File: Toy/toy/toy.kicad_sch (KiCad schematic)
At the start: 13 parts, among them J1 Conn_01x07_Pin, J2 Conn_01x03_Pin

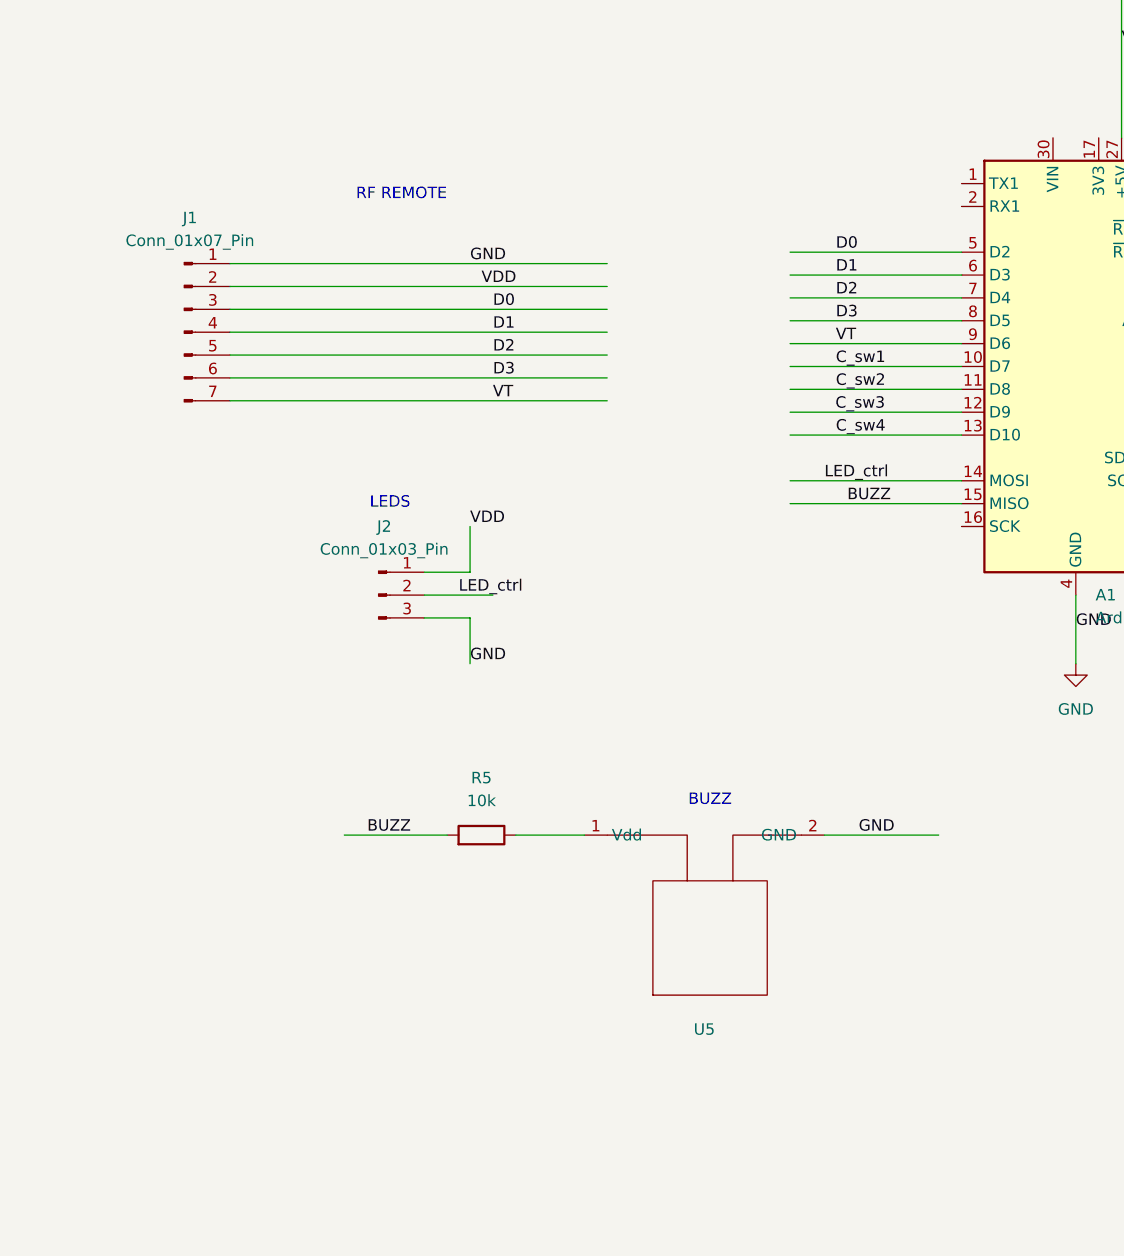
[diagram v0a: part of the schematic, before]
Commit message: V2
resistors changed
routing strategy
added more leds
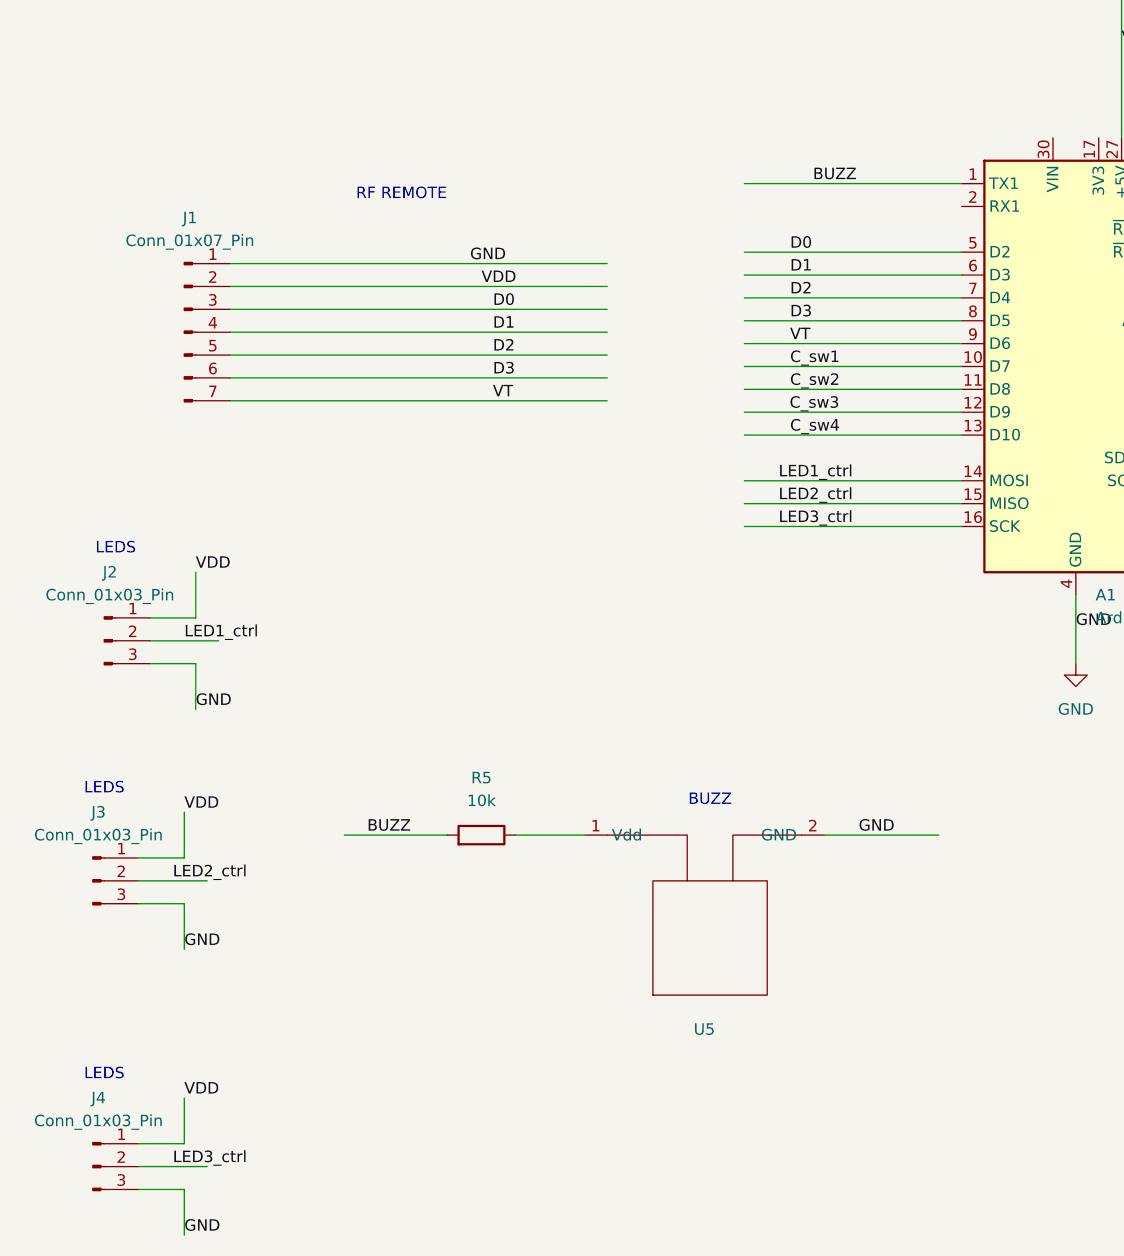
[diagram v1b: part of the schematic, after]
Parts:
- added J3, J4: Conn_01x03_Pin, Connector_PinSocket_2.54mm:PinSocket_1x03_P2.54mm_Vertical, symbol Connector:Conn_01x03_Pin
- R1, R2, R3, R4, R5: footprint Crystal:Resonator-2Pin_W6.0mm_H3.0mm -> Resistor_THT:R_Axial_DIN0207_L6.3mm_D2.5mm_P10.16mm_Horizontal
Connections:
- net BUZZ: now also A1.1 (TX1); no longer A1.15 (MISO)
- net GND: now also J3.3 (Pin_3), J4.3 (Pin_3)
- net VDD: now also J3.1 (Pin_1), J4.1 (Pin_1)
- net LED3_ctrl: now reaches A1.16 (SCK)
- net LED3_ctrl: now also J4.2 (Pin_2)
- net LED_ctrl renamed LED1_ctrl
- new net LED2_ctrl: A1.15 (MISO), J3.2 (Pin_2)
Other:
- moved on the sheet: J2

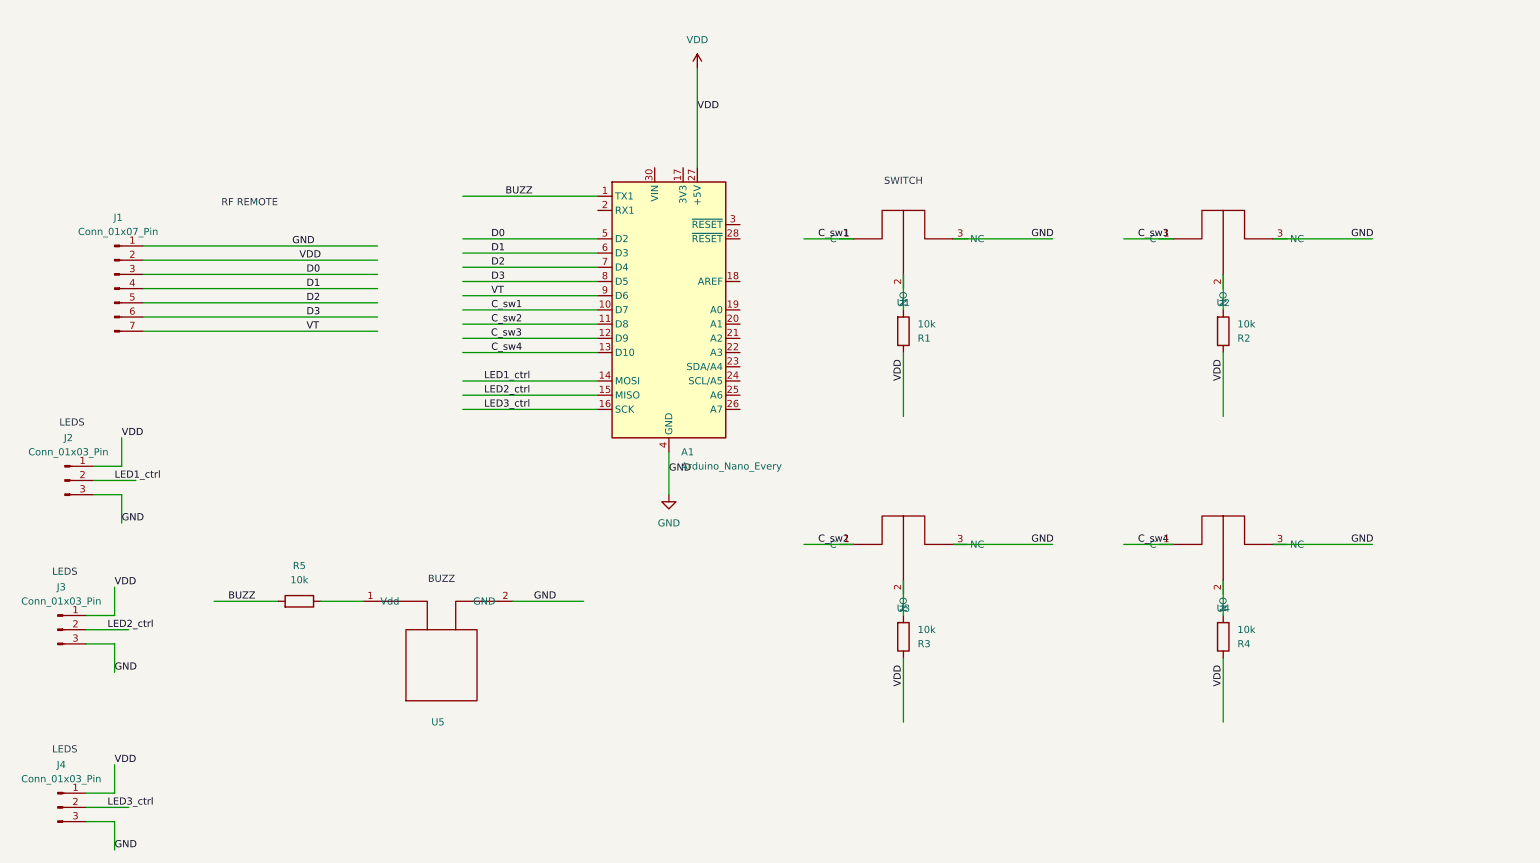
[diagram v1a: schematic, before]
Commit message: PCB updates, change switches to SPST style
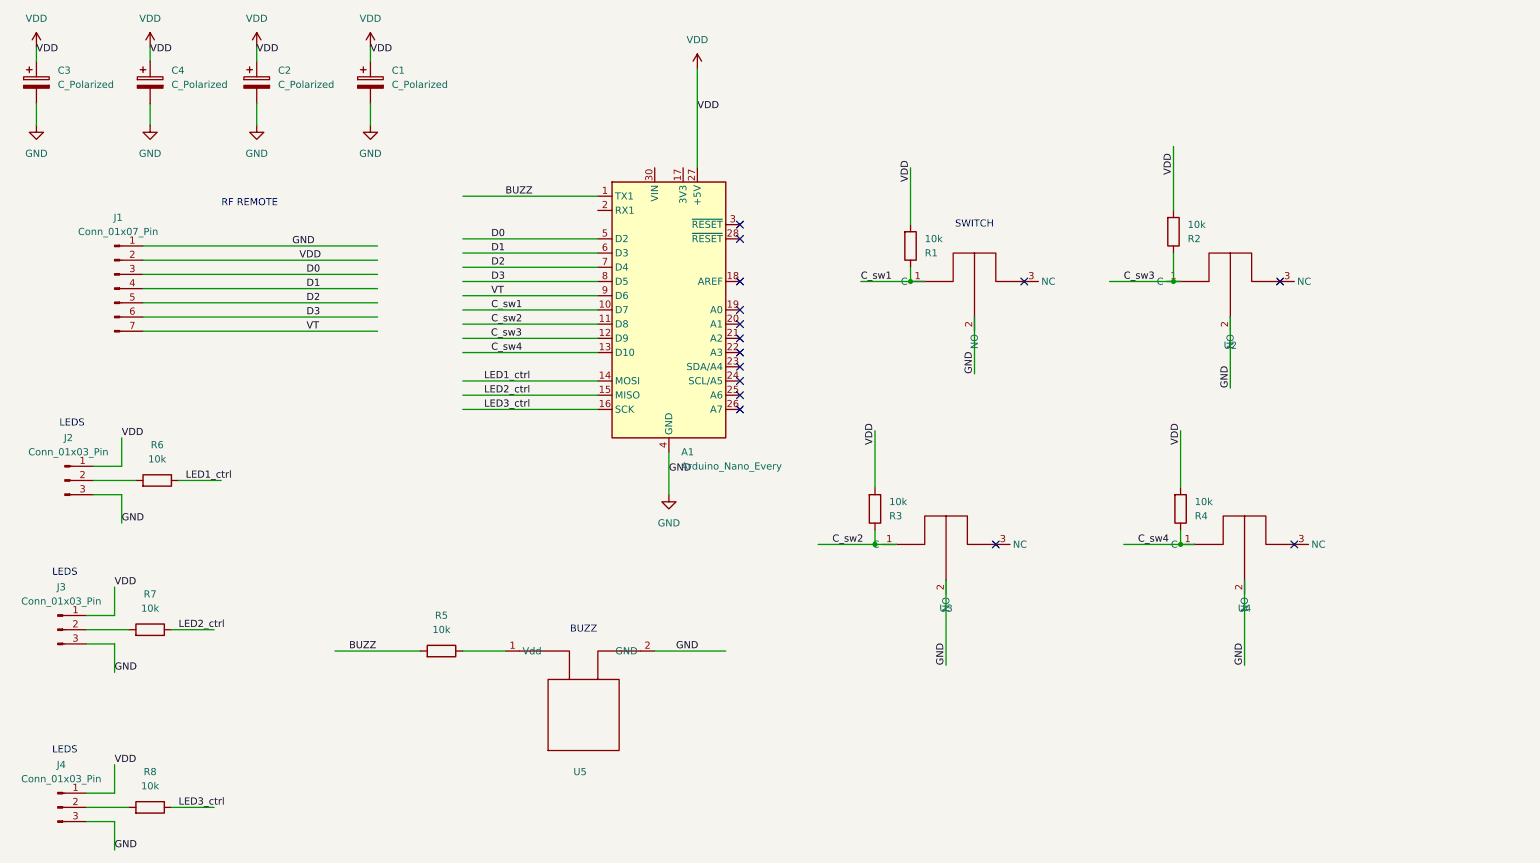
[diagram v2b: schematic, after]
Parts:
- added C1, C2, C3, C4: C_Polarized, Capacitor_THT:CP_Radial_Tantal_D5.5mm_P5.00mm, symbol Device:C_Polarized
- added R6, R7, R8: 10k, Resistor_THT:R_Axial_DIN0207_L6.3mm_D2.5mm_P10.16mm_Horizontal, symbol Device:R
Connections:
- net C_sw1: now also R1.1
- net C_sw2: now also R3.1
- net C_sw3: now also R2.1
- net C_sw4: now also R4.1
- net GND: now also U1.2 (NO), U2.2 (NO), U3.2 (NO), U4.2 (NO), C1.2, C2.2, C3.2, C4.2; no longer U1.3 (NC), U2.3 (NC), U3.3 (NC), U4.3 (NC)
- net LED1_ctrl: now also R6.1; no longer J2.2 (Pin_2)
- net LED2_ctrl: now also R7.1; no longer J3.2 (Pin_2)
- net LED3_ctrl: now also R8.1; no longer J4.2 (Pin_2)
- net VDD: now also R1.2, R2.2, R3.2, R4.2, C1.1, C2.1, C3.1, C4.1; no longer R1.1, R2.1, R3.1, R4.1
- new net: J3.2 (Pin_2), R7.2
- new net: J4.2 (Pin_2), R8.2
- new net: J2.2 (Pin_2), R6.2
- no-connect marks 0 -> 15
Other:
- moved on the sheet: R1, R2, R3, R4, R5, U2, U3, U4, U5

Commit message: PCB updates, move LEDs to same side; 6 switches; move standoff holes to edges
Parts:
- added R10, R9: 10k, Resistor_THT:R_Axial_DIN0207_L6.3mm_D2.5mm_P10.16mm_Horizontal, symbol Device:R
- added U6, U7: ~, First_cost_Library:switch, symbol Toy_needed_stuff:SW_toy
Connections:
- net GND: now also U6.2 (NO), U7.2 (NO)
- net VDD: now also R10.2, R9.2
- net C_sw5: now reaches A1.19 (A0)
- net C_sw5: now also R9.1, U6.1 (C)
- net C_sw6: now reaches A1.20 (A1)
- net C_sw6: now also R10.1, U7.1 (C)
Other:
- moved on the sheet: R2, R4, U2, U4
